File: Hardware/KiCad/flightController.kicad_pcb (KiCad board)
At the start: 4 copper layers, 57 x 57 mm, 180 parts, among them J1 USB_B_Mini, J10 JST SH1-2P, J11 MOLEX 5268-7P, J12 JST SH1-8P, J2 USB_B_Mini, J3 2.54mm header, J4 2.54mm header, J5 TF-01A, J6 1mm header, J7 JST SH1-4P, J8 JST SH1-4P, J9 JST SH1-4P, Q1 PMBT3904, Q2 PMBT3904, SW1 SW_SPDT, SW2 SW_Push, U1 MPU-6000, U10 CH330N, U11 SMF05CT1G, U12 SMF05CT1G, U13 SMF05CT1G, U2 HMC5883L, U3 FM24C64B, U4 BMP388, U5 STM32H743VIT6, U6 AMS1117-5V, U7 AMS1117-3.3, U8 SMF05CT1G, U9 SMF05CT1G

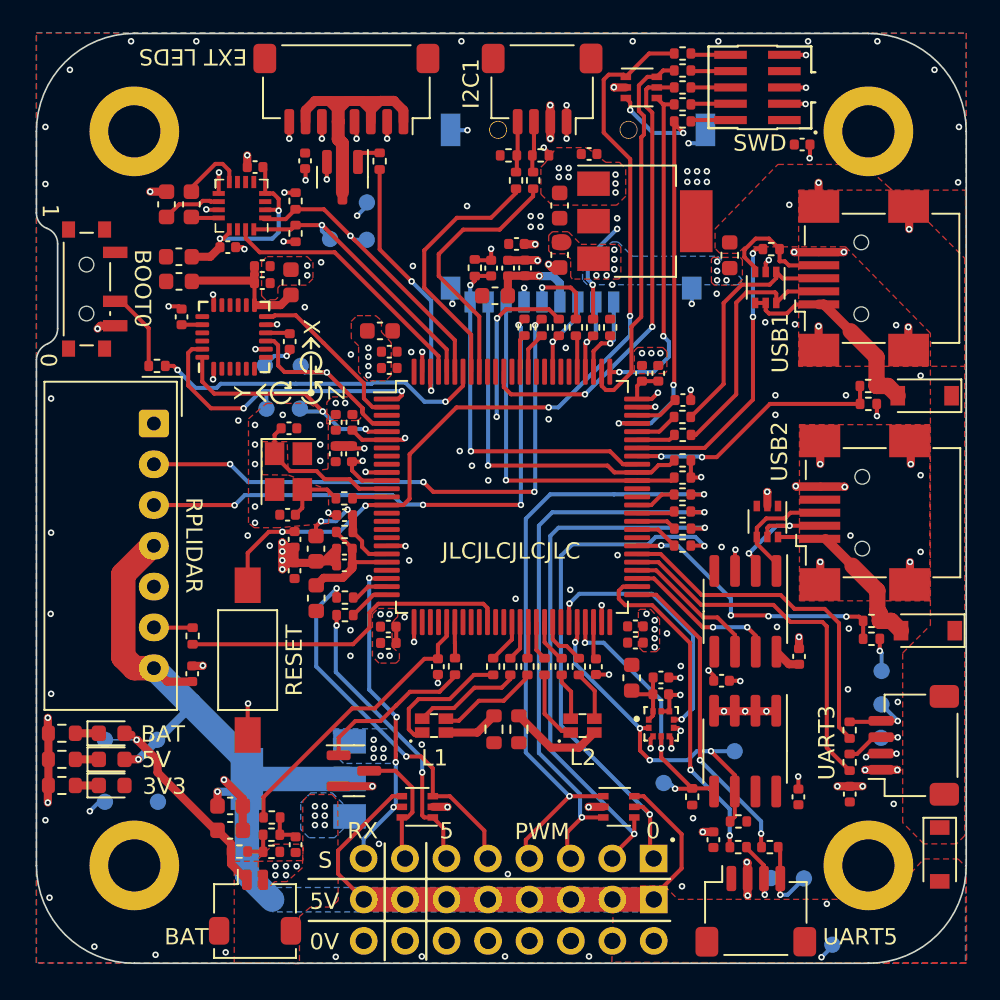
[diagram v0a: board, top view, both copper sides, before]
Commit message: Added a 5V sense line
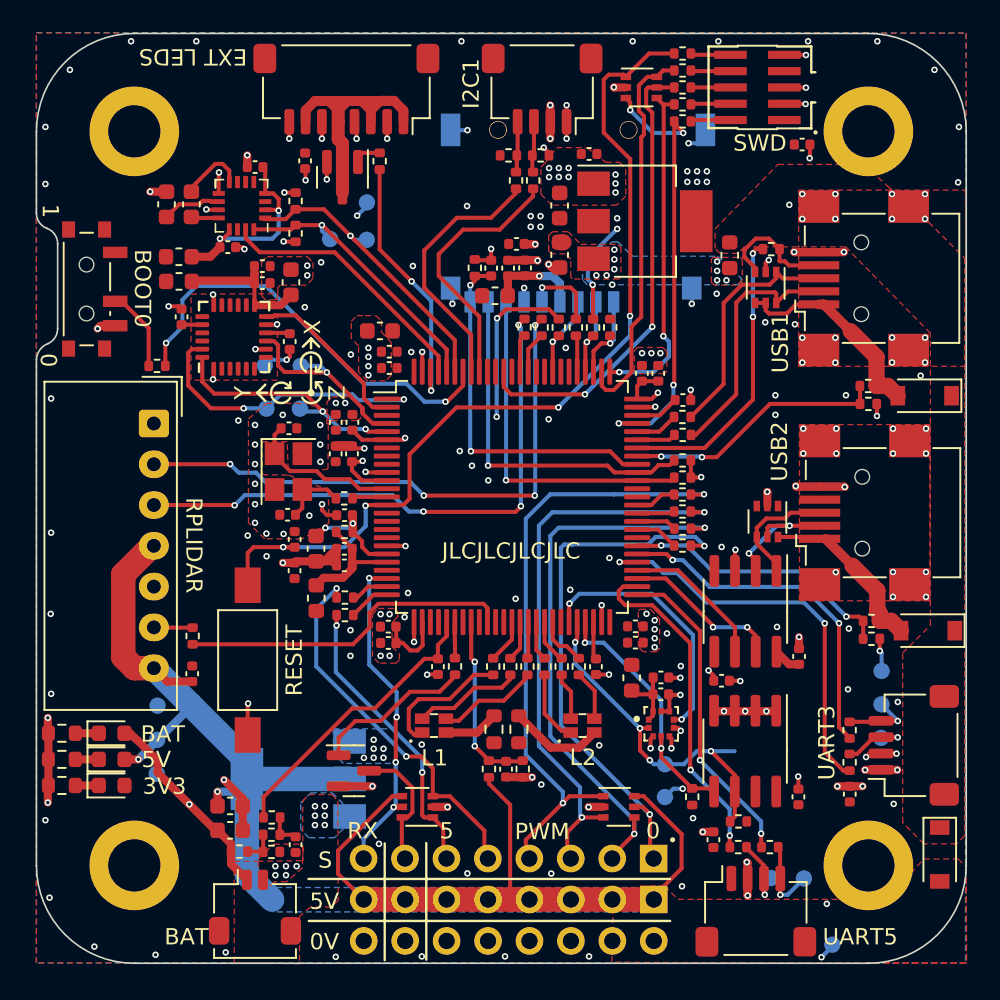
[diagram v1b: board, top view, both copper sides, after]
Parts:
- removed TP31: TestPoint, TestPoint:TestPoint_Pad_D1.0mm
- added C54: 100n, Capacitor_SMD:C_0402_1005Metric, F.Cu at (98.8, 122.1)
- added R61: 56k, Resistor_SMD:R_0402_1005Metric, F.Cu at (97.7, 122.1)
- added R62: 100k, Resistor_SMD:R_0402_1005Metric, F.Cu at (99.8, 122.1)
- moved TP29 5.90 mm to (77.4, 118.2)
- moved TP4 4.34 mm to (108.5, 121.8)
- moved TP30 3.80 mm to (77.4, 122.4)
- moved TP3 0.86 mm to (108.5, 123.8)
- turned C40 to 90 degrees
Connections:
- U5 pad 33: unconnected-(U5-Pad33) -> 5V_SENSE
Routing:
- net GND: track 108.7 -> 92.3 mm, vias 139 -> 163
- net 5V_SENSE: track 0.00 -> 11.0 mm, vias 0 -> 2
- net +5V: track 78.7 -> 86.7 mm
- net BOOT0: track 20.7 -> 26.2 mm
- net +3V3: track 43.3 -> 46.5 mm, vias 103 -> 102
- net Net-(R19-Pad2): track 22.7 -> 25.1 mm, vias 0 -> 2
- net VCC: track 13.7 -> 14.9 mm
- net IMU_SCL: track 19.4 -> 18.3 mm
- net VREF+: track 7.26 -> 6.42 mm
- net NRST: track 54.8 -> 55.5 mm
- net USB_VBUS_DEBUG: track 17.5 -> 16.9 mm, vias 4 -> 2
- net USART2_RX: track 34.4 -> 35.0 mm
- net Net-(R20-Pad2): vias 0 -> 2
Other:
- board text added: "max 4s LiPo"

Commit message: Changed the 3.3V LDO to one that supports a lower Vin so sub 5V USB supplies are less likely to pose a problem
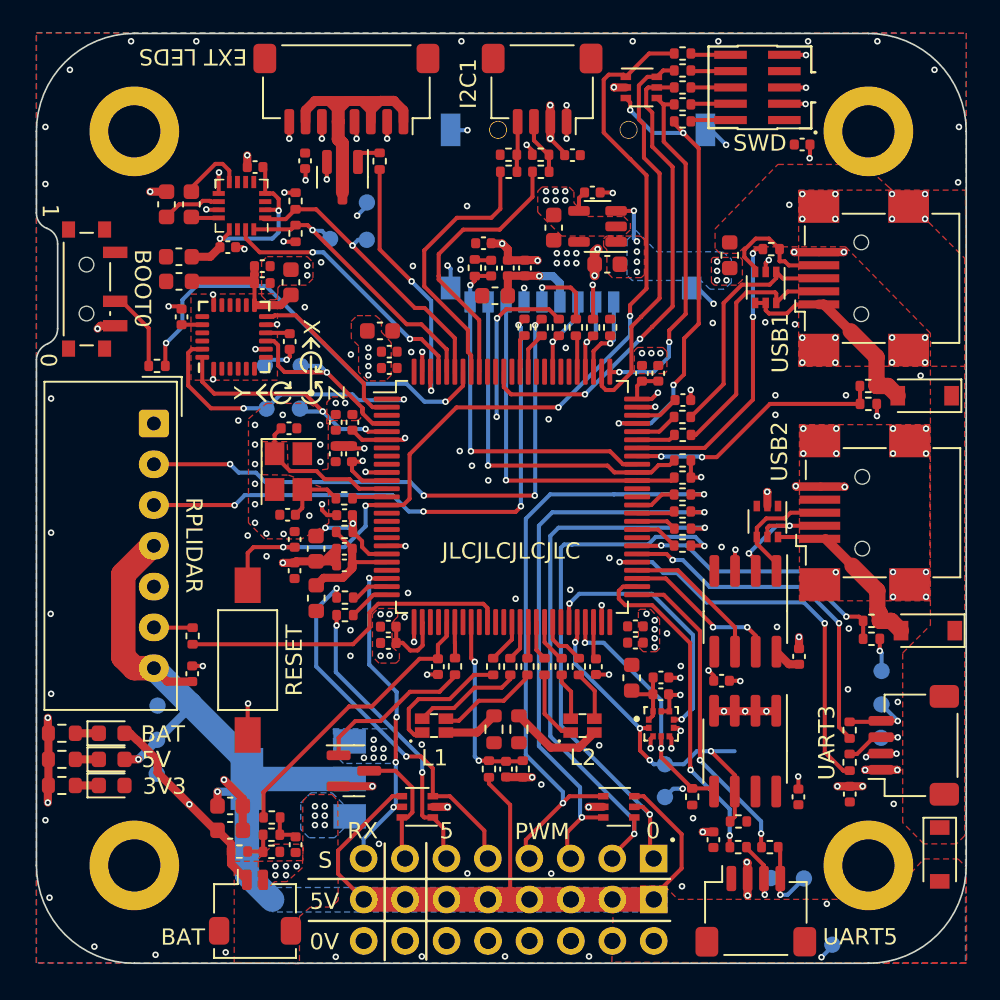
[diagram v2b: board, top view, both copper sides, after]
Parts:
- added C55: 10nF, Capacitor_SMD:C_0402_1005Metric, F.Cu at (104.1, 86.8)
- U7: value AMS1117-3.3 -> SPX3819M5-L-3-3/TR; footprint Package_TO_SOT_SMD:SOT-223-3_TabPin2 -> Package_TO_SOT_SMD:SOT-23-5
- moved C31 2.98 mm to (105.0, 91.2), turned to 180 degrees
- moved U7 2.92 mm to (104.4, 88.8), turned to 180 degrees
- moved C43 2.03 mm to (97.4, 89.9)
- moved C32 1.40 mm to (101.7, 88.9)
- moved C45 1.06 mm to (98.9, 91.4)
- moved C44 1.04 mm to (100.0, 91.4)
- moved C49 1.02 mm to (102.9, 84.5)
- moved R35 0.71 mm to (100.9, 85.5), turned to 0 degrees
- moved R36 0.70 mm to (99.0, 85.5), turned to 0 degrees
- turned R46 to 180 degrees
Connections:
- U7 pad 1: GND -> Net-(C31-Pad1)
- U7 pad 2: +3V3 -> GND
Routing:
- net GND: track 92.3 -> 99.5 mm
- net +3V3: track 46.5 -> 41.8 mm, vias 102 -> 96
- net Net-(C31-Pad1): track 0.23 -> 3.05 mm
- net Net-(C55-Pad1): track 0.00 -> 1.27 mm
- net SWO/TDO: track 28.4 -> 29.5 mm
- net Net-(R35-Pad1): track 16.0 -> 16.9 mm
- net NRST: track 55.5 -> 56.3 mm
- net SWCLK/TCK: track 20.9 -> 21.7 mm
- net TDI: track 23.8 -> 24.6 mm
- net Net-(R36-Pad1): track 16.0 -> 16.6 mm
- net I2C1_SCL: track 2.94 -> 3.50 mm
- net MAG_INT: vias 0 -> 2

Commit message: SWD was 1mm pitch and needed to be 1.27 mm
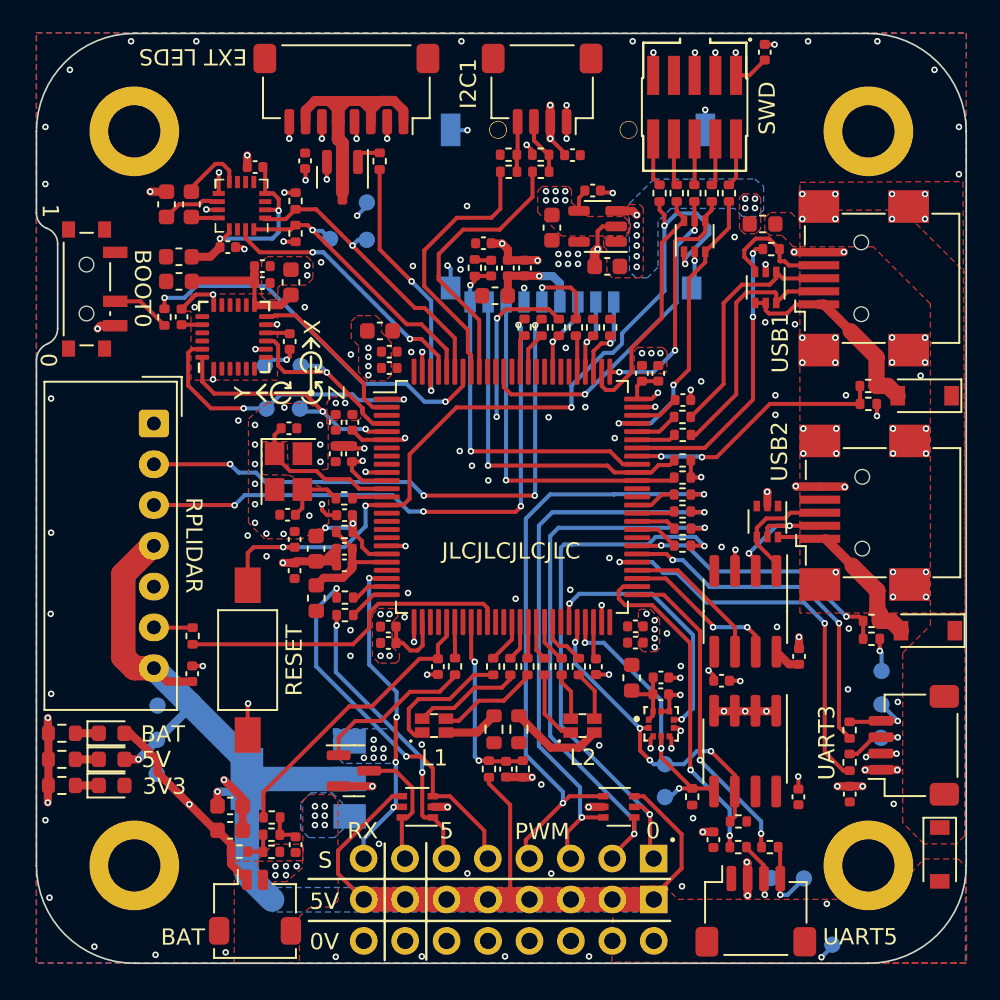
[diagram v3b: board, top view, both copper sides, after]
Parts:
- J6: footprint Connector_PinHeader_1.00mm:PinHeader_2x05_P1.00mm_Vertical_SMD -> Connector_PinHeader_1.27mm:PinHeader_2x05_P1.27mm_Vertical_SMD
- R14, R15: value 1k -> 220
- moved U13 9.69 mm to (110.3, 89.5), turned to 90 degrees
- moved R34 8.68 mm to (108.2, 86.8), turned to -90 degrees
- moved R32 7.53 mm to (109.2, 86.8), turned to -90 degrees
- moved R31 6.52 mm to (110.3, 86.8), turned to -90 degrees
- moved C47 6.11 mm to (114.7, 78.2), turned to 90 degrees
- moved R30 5.73 mm to (111.4, 86.8), turned to -90 degrees
- moved R27 5.24 mm to (112.5, 86.8), turned to -90 degrees
- moved J6 4.04 mm to (110.3, 81.5), turned to -90 degrees
- moved R48 3.02 mm to (77.8, 94.4), turned to -90 degrees
- moved FB4 2.78 mm to (114.5, 88.7), turned to 180 degrees
- moved C31 0.13 mm to (105.0, 91.3)
- moved C55 0.12 mm to (104.1, 86.7)
- moved C32 0.11 mm to (101.6, 88.9)
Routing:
- net TDI: track 24.6 -> 15.0 mm
- net SWDIO/TMS: track 28.0 -> 18.7 mm, vias 4 -> 2
- net SWO/TDO: track 29.5 -> 20.6 mm
- net SWCLK/TCK: track 21.7 -> 15.2 mm
- net NRST: track 56.3 -> 51.1 mm, vias 4 -> 5
- net BOOT0: track 26.2 -> 23.5 mm
- net GND: track 99.5 -> 101.3 mm
- net Net-(C31-Pad1): track 3.05 -> 1.37 mm, vias 9 -> 10
- net I2C2_SCL: track 21.6 -> 20.2 mm
- net +3V3: track 41.8 -> 43.2 mm, vias 96 -> 95
- net Net-(R48-Pad2): track 4.64 -> 3.63 mm
- net Net-(J6-Pad2): track 2.35 -> 2.99 mm
- net Net-(J6-Pad10): track 2.35 -> 2.97 mm
- net Net-(J6-Pad4): track 2.39 -> 2.90 mm

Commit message: Last layout optimizations and checks before production
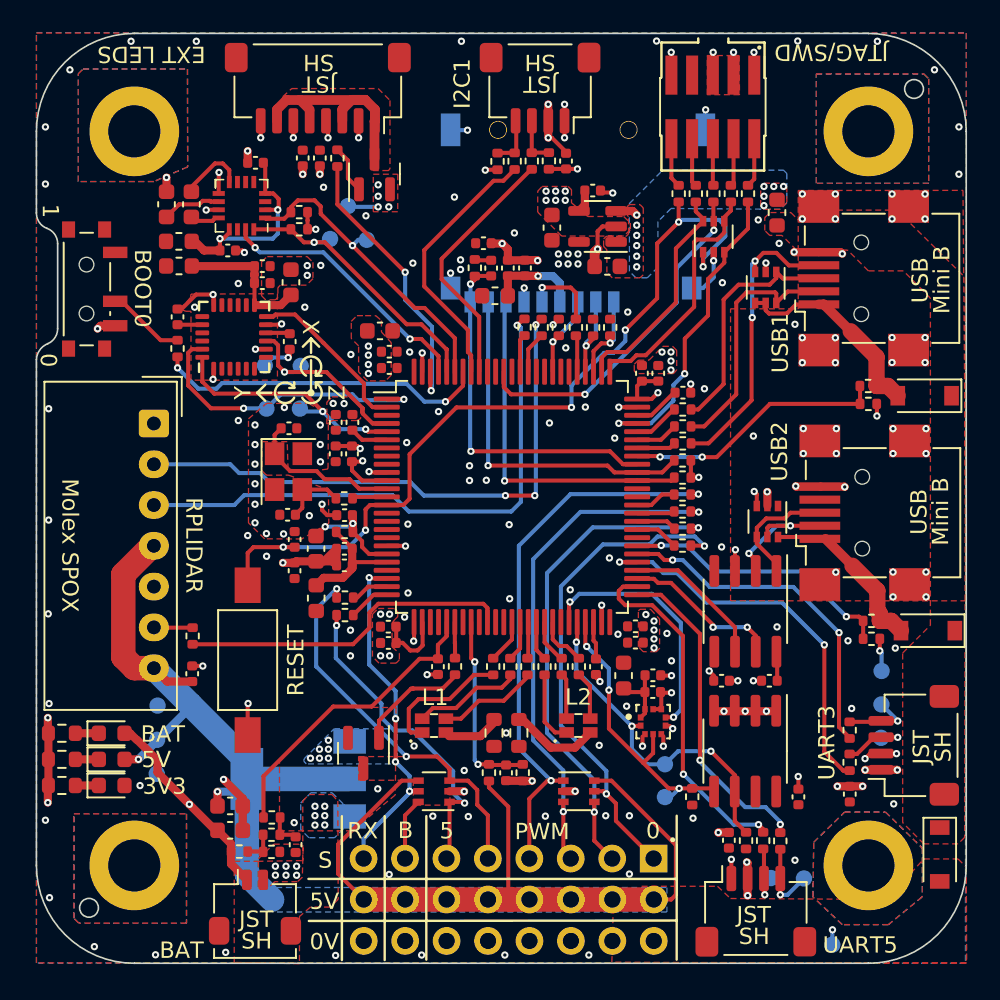
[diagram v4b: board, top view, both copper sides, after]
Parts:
- C54: value 100n -> 10n
- C55: value 10nF -> 10n
- moved C47 29.1 mm to (86.3, 84.7), turned to -90 degrees
- moved R51 13.1 mm to (109.6, 102.2)
- moved U11 2.63 mm to (103.2, 123.5)
- moved R60 2.60 mm to (88.5, 84.7)
- moved C41 2.35 mm to (114.9, 116.7), turned to 180 degrees
- moved R48 2.08 mm to (78.7, 96.3), turned to 90 degrees
- moved Q2 1.98 mm to (90.7, 85.6), turned to 90 degrees
- moved J12 1.75 mm to (87.2, 80.4)
- moved R38 1.58 mm to (114.5, 126.5), turned to -90 degrees
- moved U12 1.40 mm to (94.4, 123.5)
- moved R42 1.26 mm to (113.5, 126.5), turned to -90 degrees
- moved Q1 1.23 mm to (90.0, 121.1), turned to -90 degrees
- moved TP24 1.18 mm to (89.1, 87.6)
- moved R27 1.17 mm to (113.6, 86.8)
- moved R31 1.17 mm to (111.5, 86.8)
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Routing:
- net USB_ID: track 18.1 -> 2.40 mm, vias 2 -> 0
- net Net-(J1-Pad4): track 7.68 -> 18.6 mm, vias 0 -> 2
- net +3V3: track 43.2 -> 33.6 mm, vias 95 -> 110
- net Net-(J12-Pad1): track 19.5 -> 13.4 mm
- net BUZZ_IN: track 7.93 -> 3.82 mm
- net +5V: track 86.7 -> 90.7 mm
- net PWM3: track 37.8 -> 34.2 mm
- net PWM1: track 34.2 -> 30.7 mm
- net PWM2: track 34.5 -> 31.1 mm
- net GND: track 101.3 -> 98.2 mm, vias 163 -> 167
- net Net-(Q1-Pad1): track 9.77 -> 6.85 mm
- net BOOT0: track 23.5 -> 20.6 mm
- net PWM5: track 18.0 -> 19.8 mm
- net PWM0: track 32.7 -> 31.0 mm
- net Net-(Q2-Pad1): track 1.44 -> 2.97 mm
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- added copper zone on F.Cu, net BUZZ_IN
- added copper zone on F.Cu, net Net-(J12-Pad1)
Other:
- outline, holes or cut-outs redrawn
- board text added: "B"
- board text added: "JST"
- board text added: "JTAG/SWD"
- board text added: "Mini B"
- board text added: "Molex SPOX"
- board text added: "NR:"
- board text added: "SH"
- board text added: "USB"
- board text removed: "SWD"

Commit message: Updated BOM table
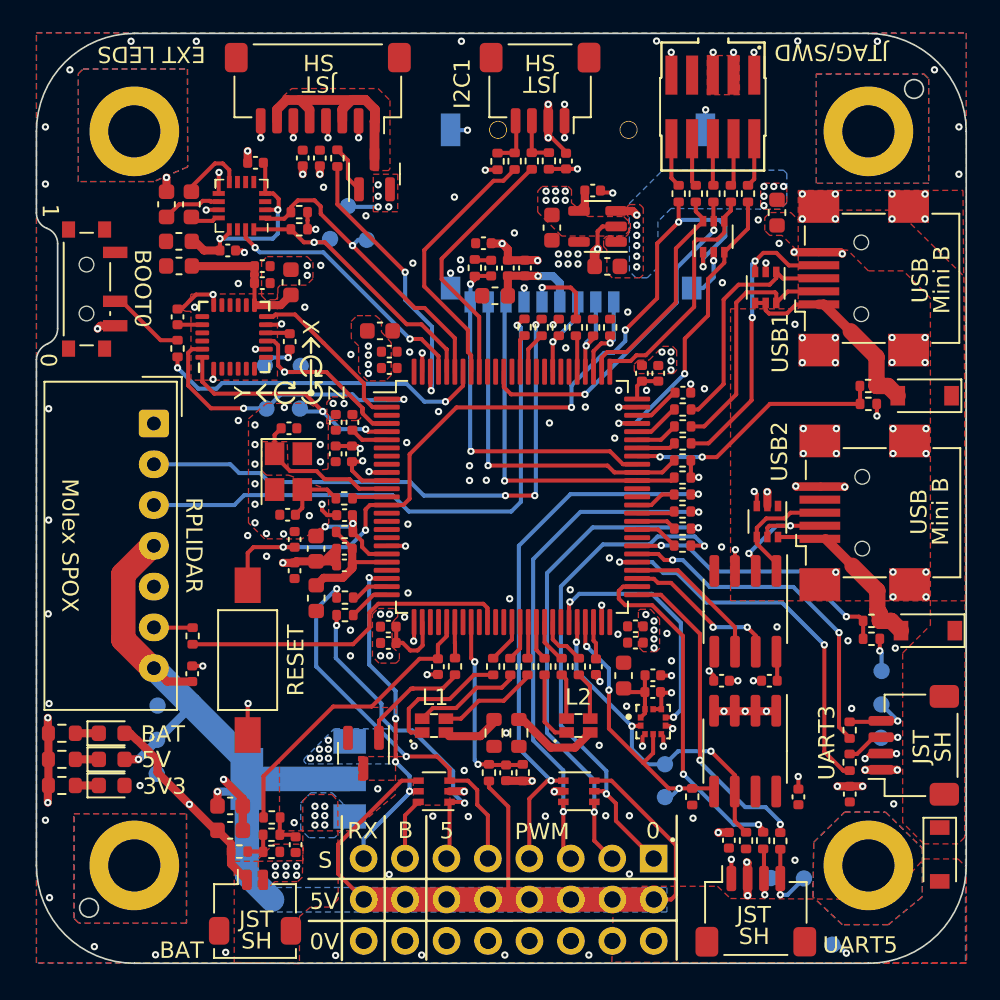
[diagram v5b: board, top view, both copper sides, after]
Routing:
- net +3V3: track 33.6 -> 32.2 mm, vias 110 -> 109
- net +5V: track 90.7 -> 90.0 mm
- net SWDIO/TMS: track 19.1 -> 18.6 mm
